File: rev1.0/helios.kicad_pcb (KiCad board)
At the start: 4 copper layers, 16.4 x 43.4 mm, 57 parts, among them J1 USB_C_Receptacle_USB2.0, J2 helios-pinout, Q1 2N7002VC-, Q2 2N7002VC-, SW1 SWITCH, U1 USBLC6-2P6, U2 TLV75533PDQNR, U3 W25Q128JVPIQ, U4 RP2040, U5 74LVC1T45, Y1 12MHz

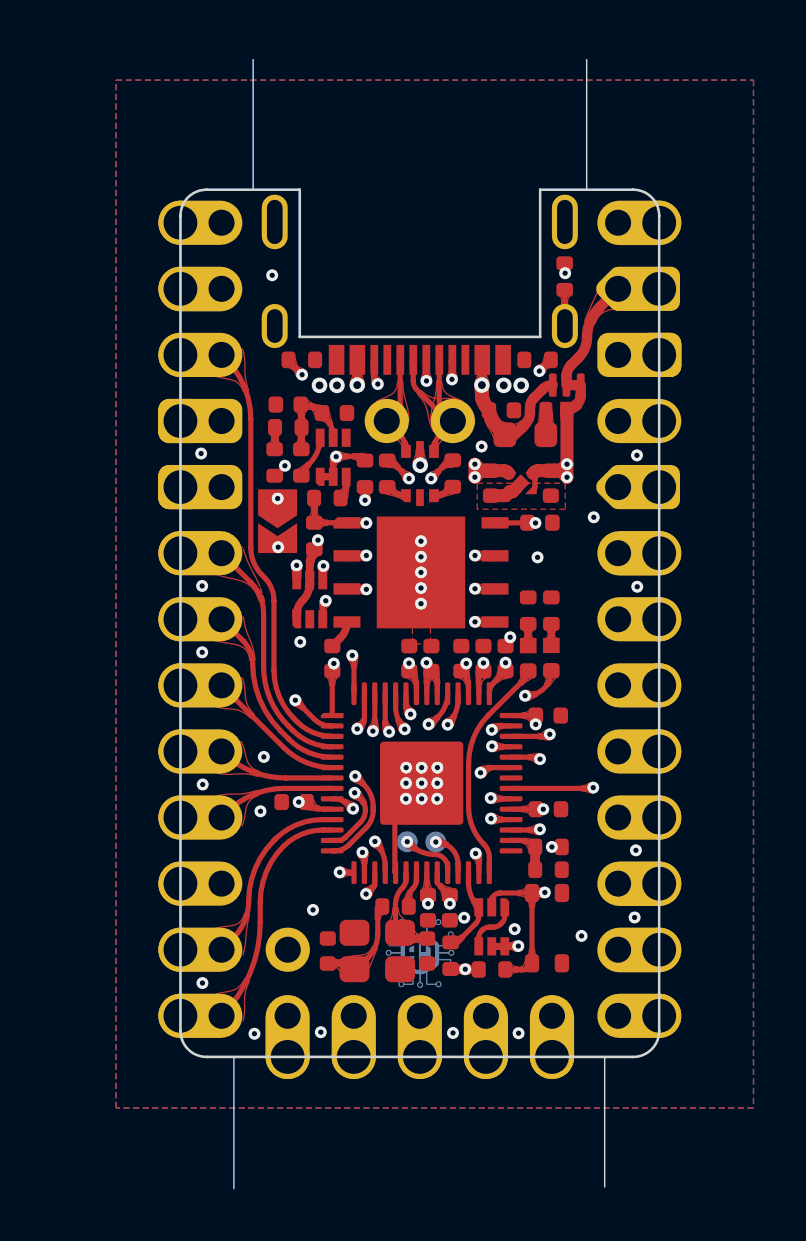
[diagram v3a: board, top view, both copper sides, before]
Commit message: Fix readme and add current prod
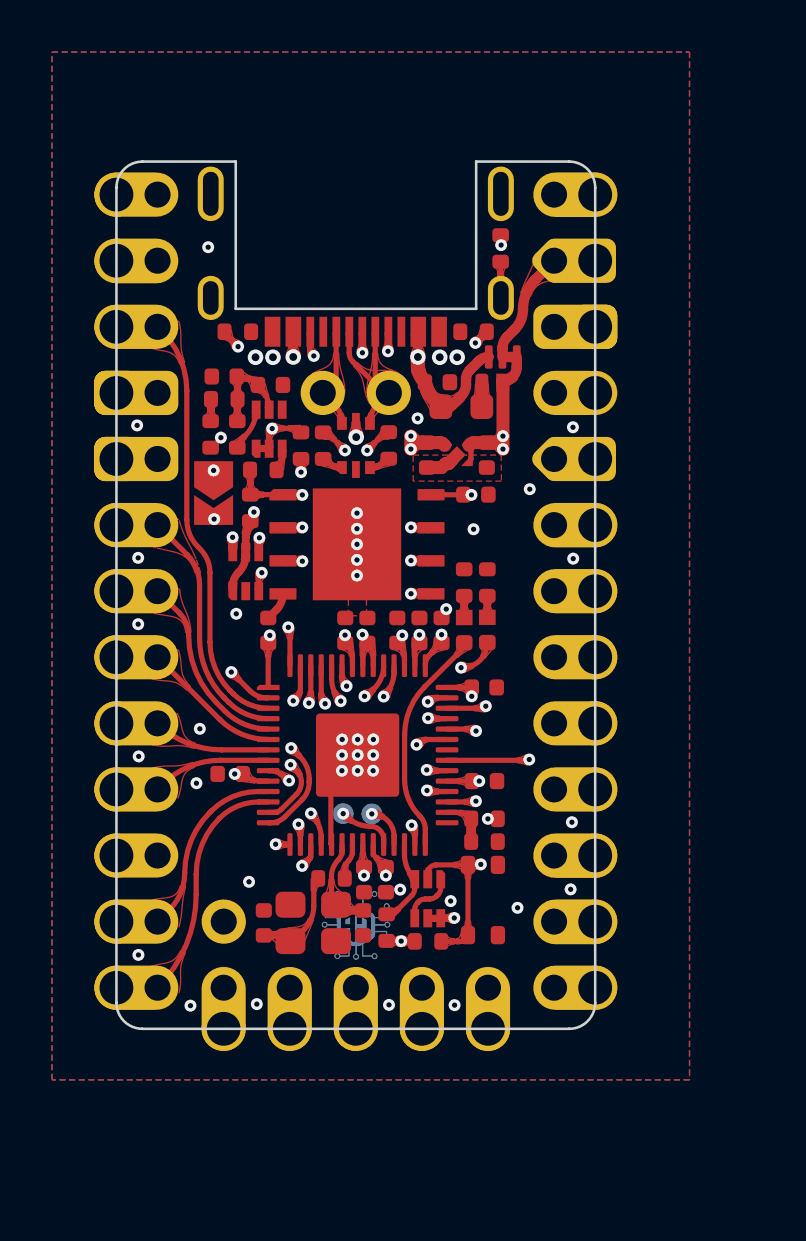
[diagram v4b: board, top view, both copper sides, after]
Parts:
- added REF**: Tab, kikit:Tab, F.Cu at (69.3, 81.3)
- added REF**: Tab, kikit:Tab, F.Cu at (82.6, 81.3)
- added REF**: Tab, kikit:Tab, F.Cu at (83.2, 115.3)
- added REF**: Tab, kikit:Tab, F.Cu at (68.7, 115.4)
- C1: value 4.7u -> 4u7
- R12, R13: value 27 -> 27R
- R16, R7, R8: value 5.1k -> 5k1
- R4, R5, R6: value 51k -> 51K
- R9: value 1k -> 1K
- moved R10 2.69 mm to (81.0, 98.0)
- moved R15 2.69 mm to (80.1, 98.0)
- moved R7 2.69 mm to (80.5, 88.3)
- moved TP2 2.69 mm to (76.5, 106.8)
- moved C1 2.69 mm to (70.9, 90.0)
- moved C12 2.69 mm to (80.9, 105.6)
- moved C14 2.69 mm to (76.4, 99.8)
- moved C16 2.69 mm to (72.6, 99.8)
- moved C3 2.69 mm to (79.1, 90.3)
- moved C4 2.69 mm to (81.0, 93.1)
- moved C6 2.69 mm to (80.5, 94.6)
- moved C7 2.69 mm to (76.2, 111.0)
- moved C9 2.69 mm to (78.4, 99.8)
- moved D1 2.69 mm to (81.0, 99.8)
- moved D2 2.69 mm to (80.1, 99.8)
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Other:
- board size 16.4 x 43.4 mm -> 18.4 x 33.3 mm
